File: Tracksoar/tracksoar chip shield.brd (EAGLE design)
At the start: 43.7 x 19.6 mm, 5 parts

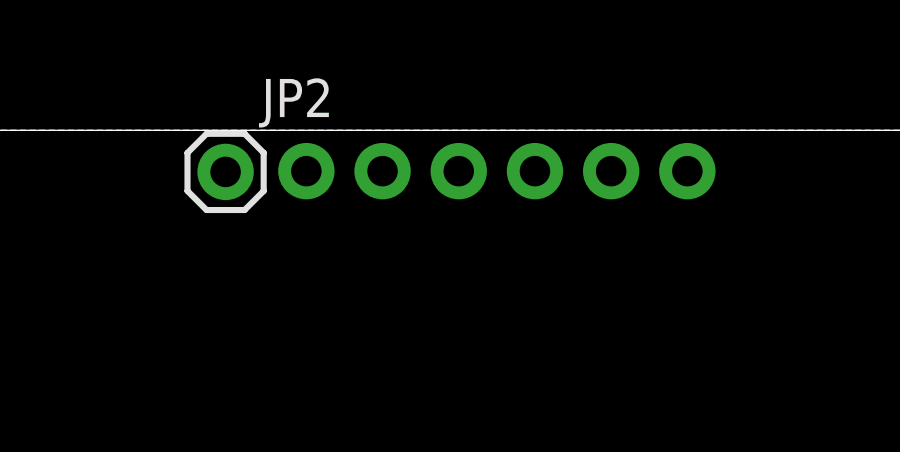
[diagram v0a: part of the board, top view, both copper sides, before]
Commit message: replace headers
replaced 2.54mm headers on all production boards with 2mm headers to
resolve daughter board issues.
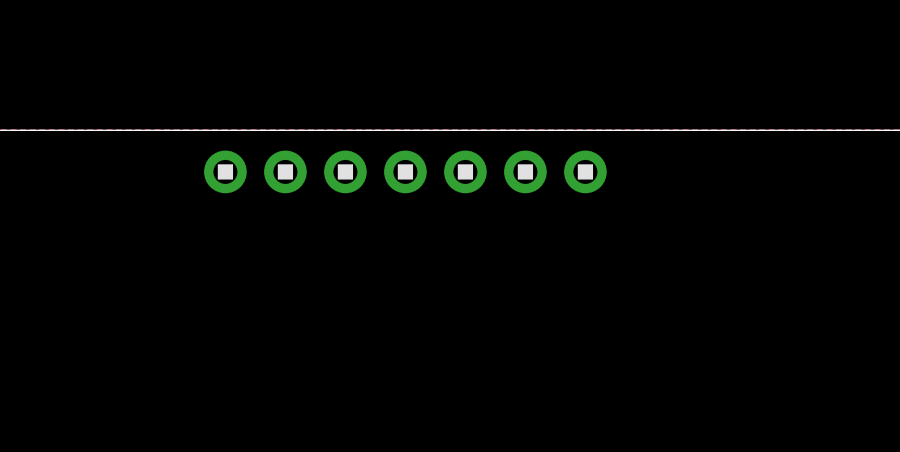
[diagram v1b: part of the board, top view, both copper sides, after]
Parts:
- removed FTDI: (no value), SparkFun-Connectors:1X06_NO_SILK
- removed JP2: (no value), SparkFun-Connectors:1X01
- added U$1: 1X7, headers(2mm):1X7
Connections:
- net !RESET: now also U$1.7; no longer JP2.1
- net DTR: now also U$1.6; no longer FTDI.1
- net GND: now also U$1.1, U$1.2; no longer FTDI.5, FTDI.6
- net RXO: now also U$1.5; no longer FTDI.2
- net TXO: now also U$1.4; no longer FTDI.3
- net VCC: now also U$1.3; no longer FTDI.4
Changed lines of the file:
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@@
 </autorouter>
 <elements>
-<element name="FTDI" library="SparkFun-Connectors" package="1X06_NO_SILK" value="" x="12.9794" y="17.8562" rot="MR180">
-<attribute name="PROD_ID" value="CONN-08437" x="12.9794" y="17.8562" size="1.778" layer="28" rot="MR180" display="off"/>
-</element>
 <element name="SPI" library="SparkFun-Connectors" package="JST-4-PTH-VERT" value="" x="20.0914" y="1.651"/>
 <element name="FRAME1" library="SparkFun-Aesthetics" package="CREATIVE_COMMONS" value="FRAME-LETTER" x="14.3764" y="-8.1534"/>
 <element name="TX1" library="SparkFun-Connectors" package="JST-2-PTH-VERT" value="TX" x="14.1478" y="1.651"/>
-<element name="JP2" library="SparkFun-Connectors" package="1X01" value="" x="10.287" y="17.8308"/>
+<element name="U$1" library="headers(2mm)" package="1X7" value="1X7" x="16.2814" y="17.8308" rot="R180"/>
 </elements>
 <signals>
 <signal name="GND">
-<contactref element="FTDI" pad="6"/>
-<contactref element="FTDI" pad="5"/>
 <polygon width="0.4064" layer="1">
 <vertex x="-0.4064" y="19.2278"/>
@@
 <vertex x="-0.3556" y="3.429"/>
 </polygon>
+<contactref element="U$1" pad="1"/>
+<contactref element="U$1" pad="2"/>
+<wire x1="20.2814" y1="17.8308" x2="22.2814" y2="17.8308" width="0" layer="19" extent="1-1"/>
 </signal>
 <signal name="VCC">
-<contactref element="FTDI" pad="4"/>
+<contactref element="U$1" pad="3"/>
 </signal>
 <signal name="DTR">
-<contactref element="FTDI" pad="1"/>
+<contactref element="U$1" pad="6"/>
 </signal>
 <signal name="RXO">
-<contactref element="FTDI" pad="2"/>
+<contactref element="U$1" pad="5"/>
 </signal>
 <signal name="TXO">
-<contactref element="FTDI" pad="3"/>
+<contactref element="U$1" pad="4"/>
 </signal>
 <signal name="MISO">
@@
 </signal>
 <signal name="!RESET">
-<contactref element="JP2" pad="1"/>
+<contactref element="U$1" pad="7"/>
 </signal>
 </signals>
